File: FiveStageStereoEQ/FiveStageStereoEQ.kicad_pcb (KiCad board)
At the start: 2 copper layers, 124 parts, among them J101 AudioJack3, J102 AudioJack3, J201 Screw_Terminal_01x03, U201 L7812CV, U301 LM833, U302 LM833, U303 LM833, U304 LM833, U305 LM833, U306 LM833, U307 LM833

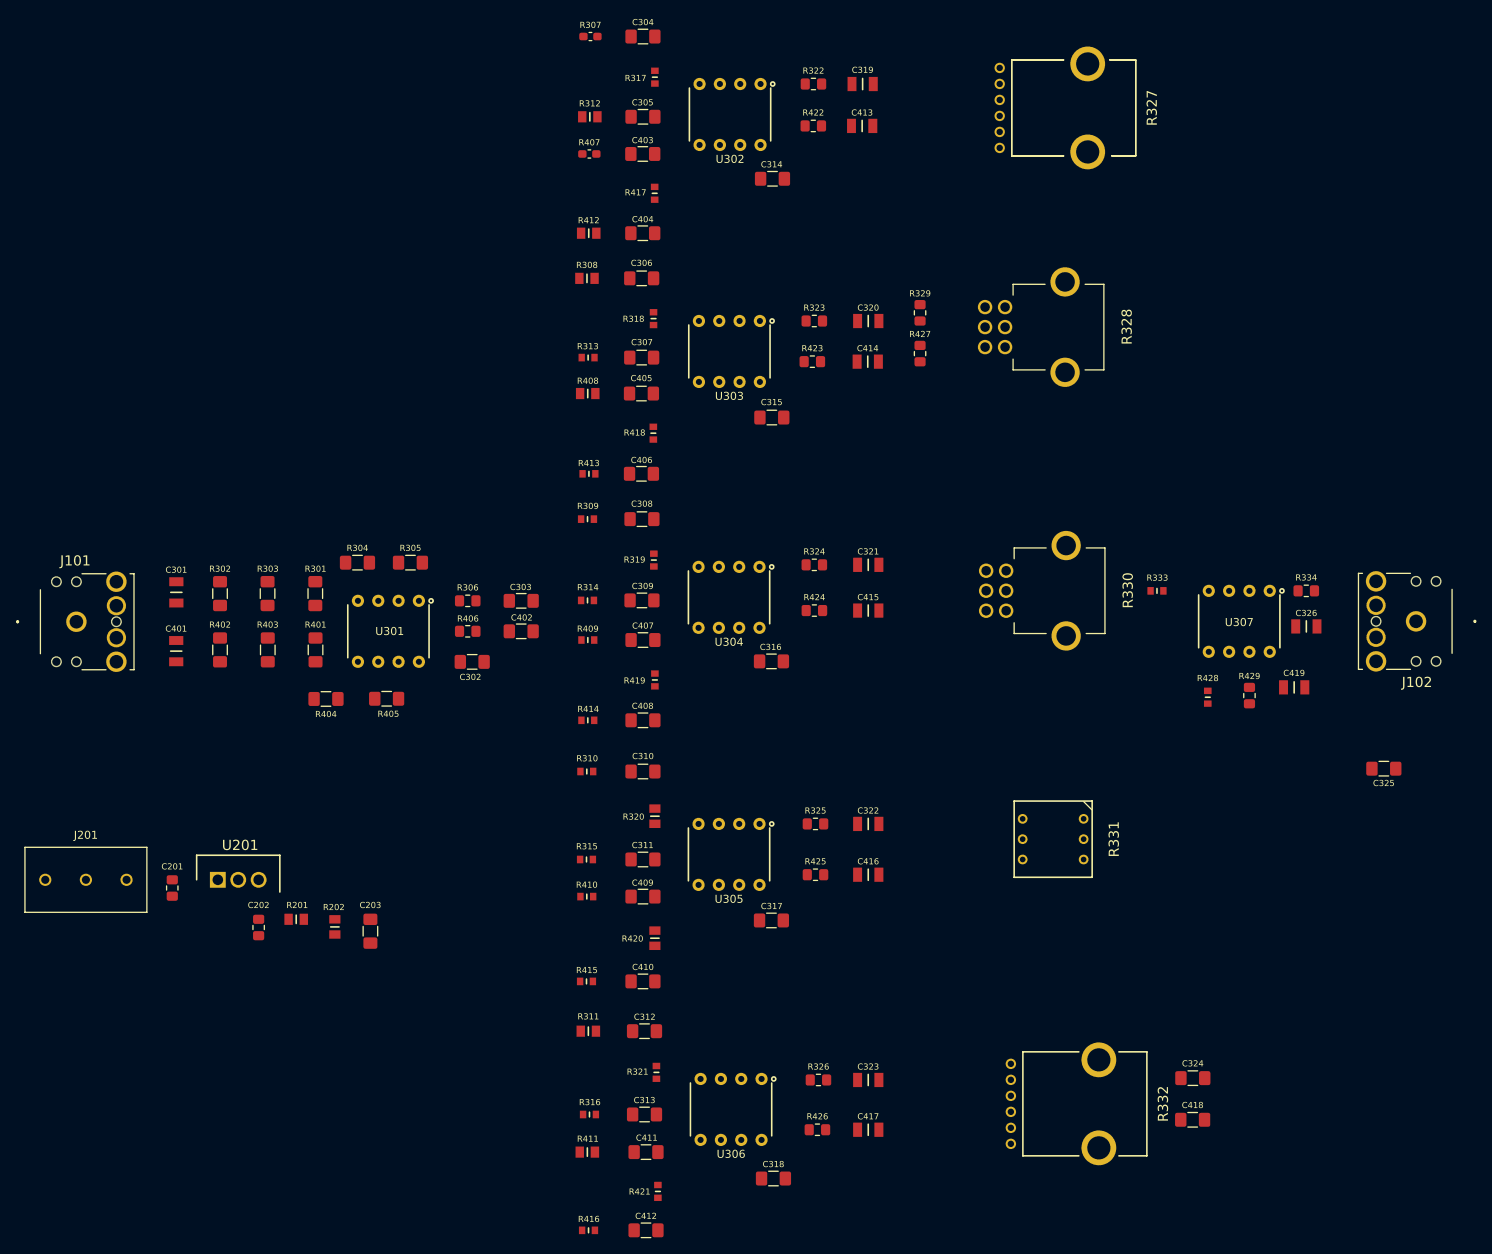
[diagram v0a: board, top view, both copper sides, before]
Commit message: almost finished, need to fix audio jack footprint
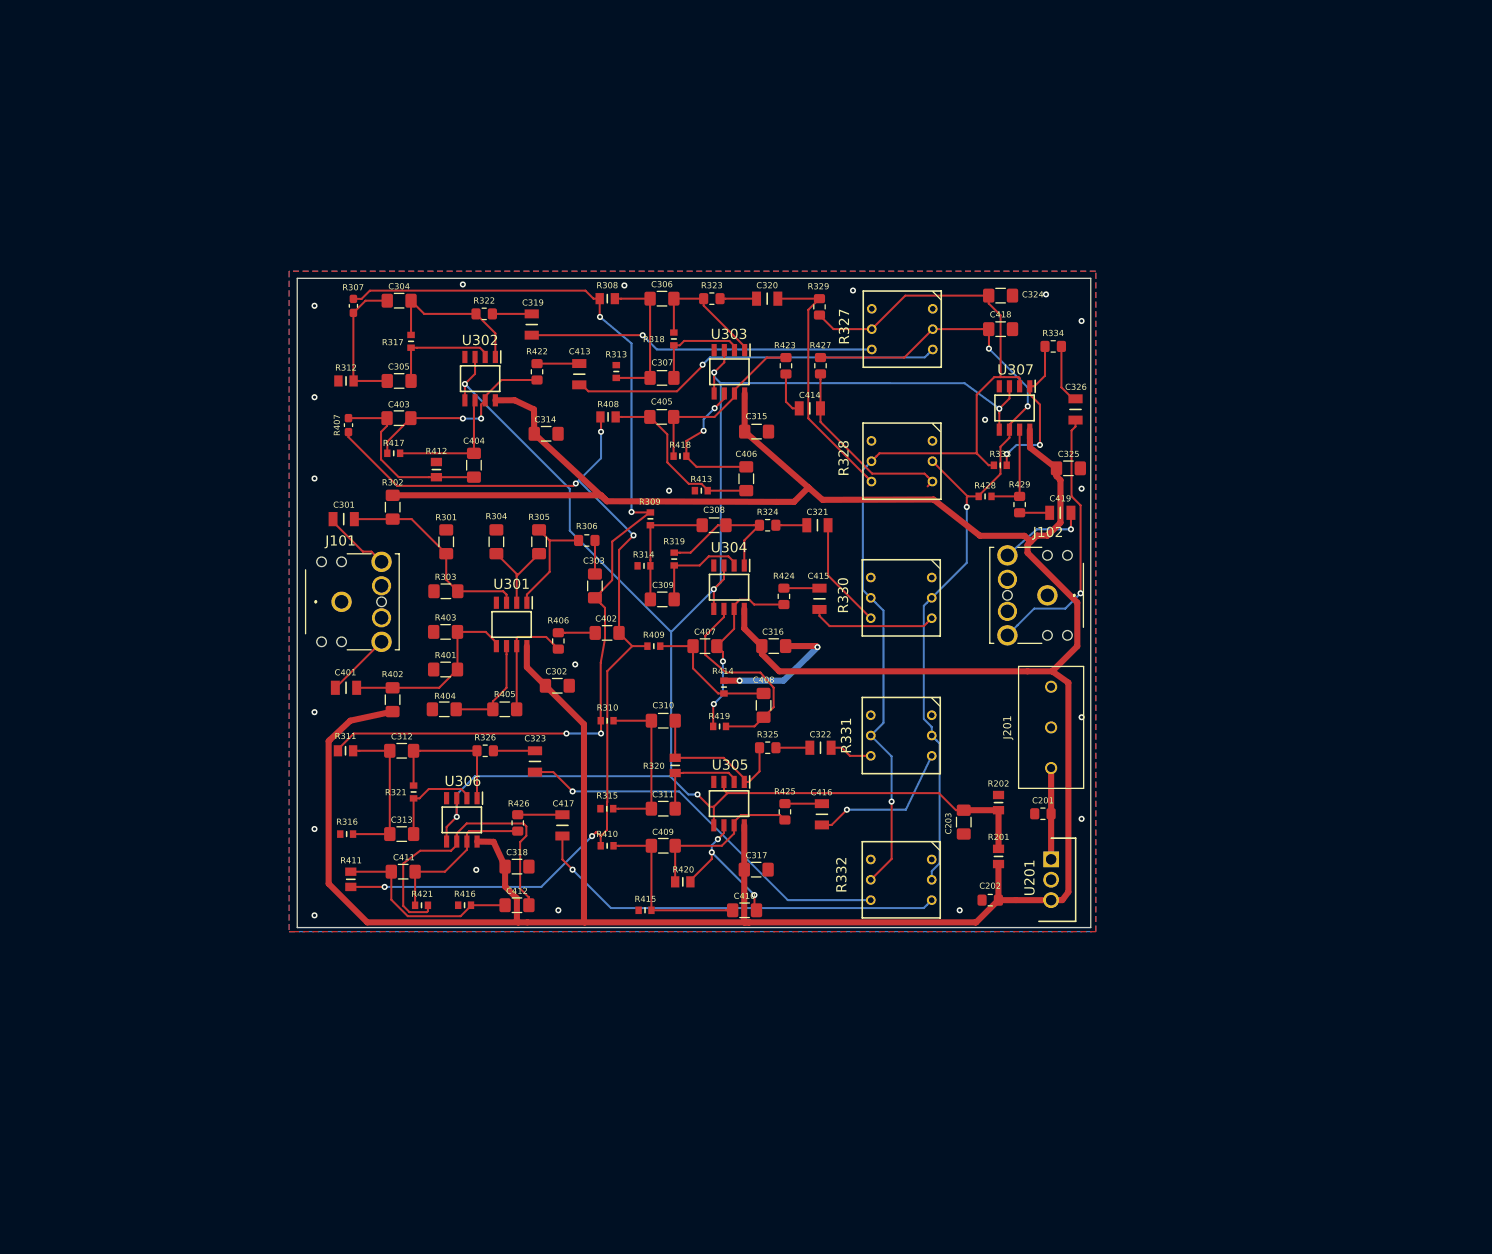
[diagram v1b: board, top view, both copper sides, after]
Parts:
- R327: footprint SamacSys_Parts:RK12L12C0A0G -> SamacSys_Parts:3310H001202L
- R328, R330: footprint SamacSys_Parts:P0925NFC15BR1K -> SamacSys_Parts:3310H001202L
- R332: footprint SamacSys_Parts:RK12L12C0C0P -> SamacSys_Parts:3310H001202L
- U301, U302, U303, U304, U305, U306, U307: footprint LM833_Badge:LM833-N-PDIP -> SamacSys_Parts:SOIC127P600X175-8N
- moved J201 122.1 mm to (176.5, 109.9), turned to 270 degrees
- moved C201 109.2 mm to (175.5, 120.7), turned to 180 degrees
- moved U201 104.2 mm to (176.5, 126.3), turned to 270 degrees
- moved C418 101.7 mm to (170.2, 60.1)
- moved C324 100.7 mm to (170.2, 55.9)
- moved C202 91.5 mm to (168.9, 131.4), turned to 180 degrees
- moved R201 88.1 mm to (170.0, 126.0), turned to 270 degrees
- moved R202 84.4 mm to (170.0, 119.3), turned to 270 degrees
- moved C203 75.4 mm to (165.6, 121.7)
- moved R326 58.6 mm to (105.8, 112.8)
- moved C323 57.6 mm to (112.0, 114.1), turned to 90 degrees
- moved C325 54.4 mm to (178.7, 77.5)
- moved C417 53.9 mm to (115.4, 122.1), turned to 90 degrees
- moved R426 53.6 mm to (109.9, 121.8), turned to 90 degrees
- moved C319 51.1 mm to (111.6, 59.5), turned to 90 degrees
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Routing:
- net +12V: track 0.00 -> 420.9 mm
- net V_GND: track 0.00 -> 244.1 mm, vias 0 -> 6
- net Net-(C402-Pad1): track 0.00 -> 129.2 mm, vias 0 -> 5
- net Net-(C303-Pad1): track 0.00 -> 128.1 mm, vias 0 -> 4
- net Net-(C324-Pad1): track 0.00 -> 122.1 mm, vias 0 -> 1
- net Net-(C418-Pad1): track 0.00 -> 107.0 mm, vias 0 -> 3
- net Net-(C417-Pad1): track 0.00 -> 52.0 mm, vias 0 -> 1
- net Net-(C323-Pad1): track 0.00 -> 48.6 mm, vias 0 -> 1
- net Net-(C413-Pad1): track 0.00 -> 46.8 mm, vias 0 -> 1
- net Net-(C319-Pad1): track 0.00 -> 43.2 mm, vias 0 -> 1
- net Net-(C412-Pad1): track 0.00 -> 40.2 mm
- net Ring_out: track 0.00 -> 33.6 mm, vias 0 -> 1
- net Net-(C320-Pad1): track 0.00 -> 31.9 mm
- net Net-(C408-Pad1): track 0.00 -> 26.3 mm
- net Net-(C301-Pad1): track 0.00 -> 25.9 mm
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- added copper zone on B.Cu, net GND
- added copper zone on F.Cu, net GND
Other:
- board outline added: 99.2 x 81.2 mm

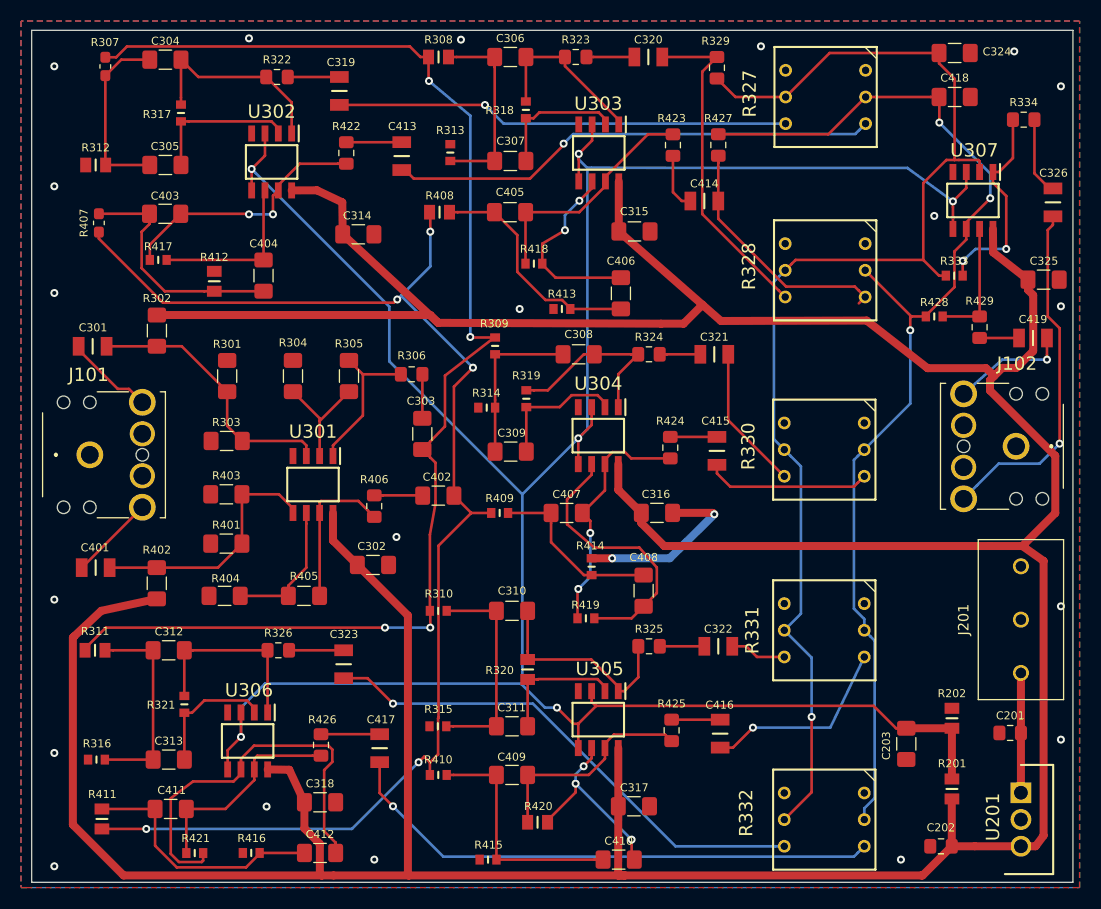
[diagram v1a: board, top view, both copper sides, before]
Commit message: fixed audio jack footprint, added better 3d jack model, added graoe nut logo on bottom silkscree and added gerbers
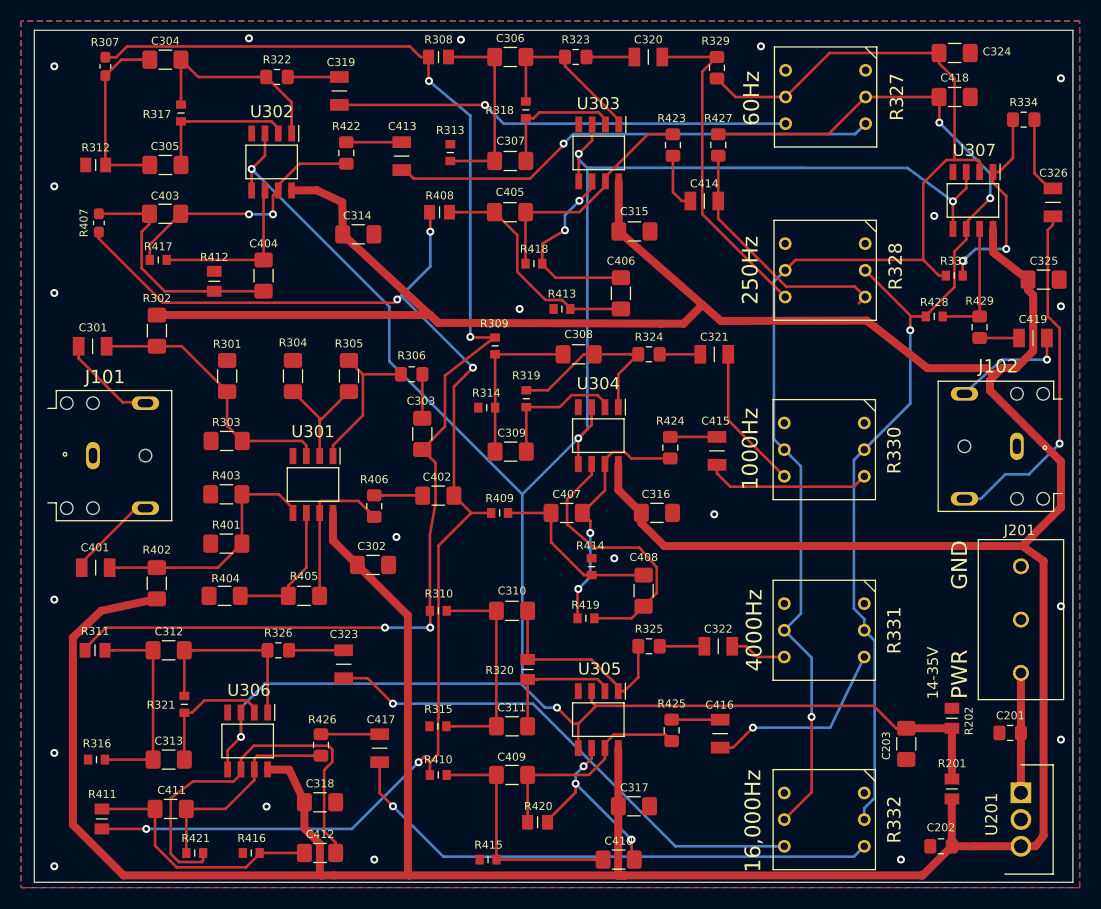
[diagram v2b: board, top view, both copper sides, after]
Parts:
- J101, J102: footprint SamacSys_Parts:SJ13523N -> SJ1-3523N:CUI_SJ1-3523N
- moved J101 4.80 mm to (88.1, 94.2)
- moved J102 4.42 mm to (176.1, 93.3)
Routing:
- net GND: track 17.4 -> 0.00 mm, vias 22 -> 21
- net Ring_in: track 8.47 -> 10.3 mm
- net Tip_in: track 8.16 -> 9.52 mm
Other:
- board size 99.2 x 81.2 mm -> 98.9 x 81.2 mm
- board text added: "1000Hz"
- board text added: "14-35V"
- board text added: "16,000Hz"
- board text added: "250Hz"
- board text added: "4000Hz"
- board text added: "60Hz"
- board text added: "GND"
- board text added: "PWR"
